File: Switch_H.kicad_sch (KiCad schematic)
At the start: 10 parts, among them Q501 NMOS, Q502 NMOS, U501 LM74700, U502 LM74700

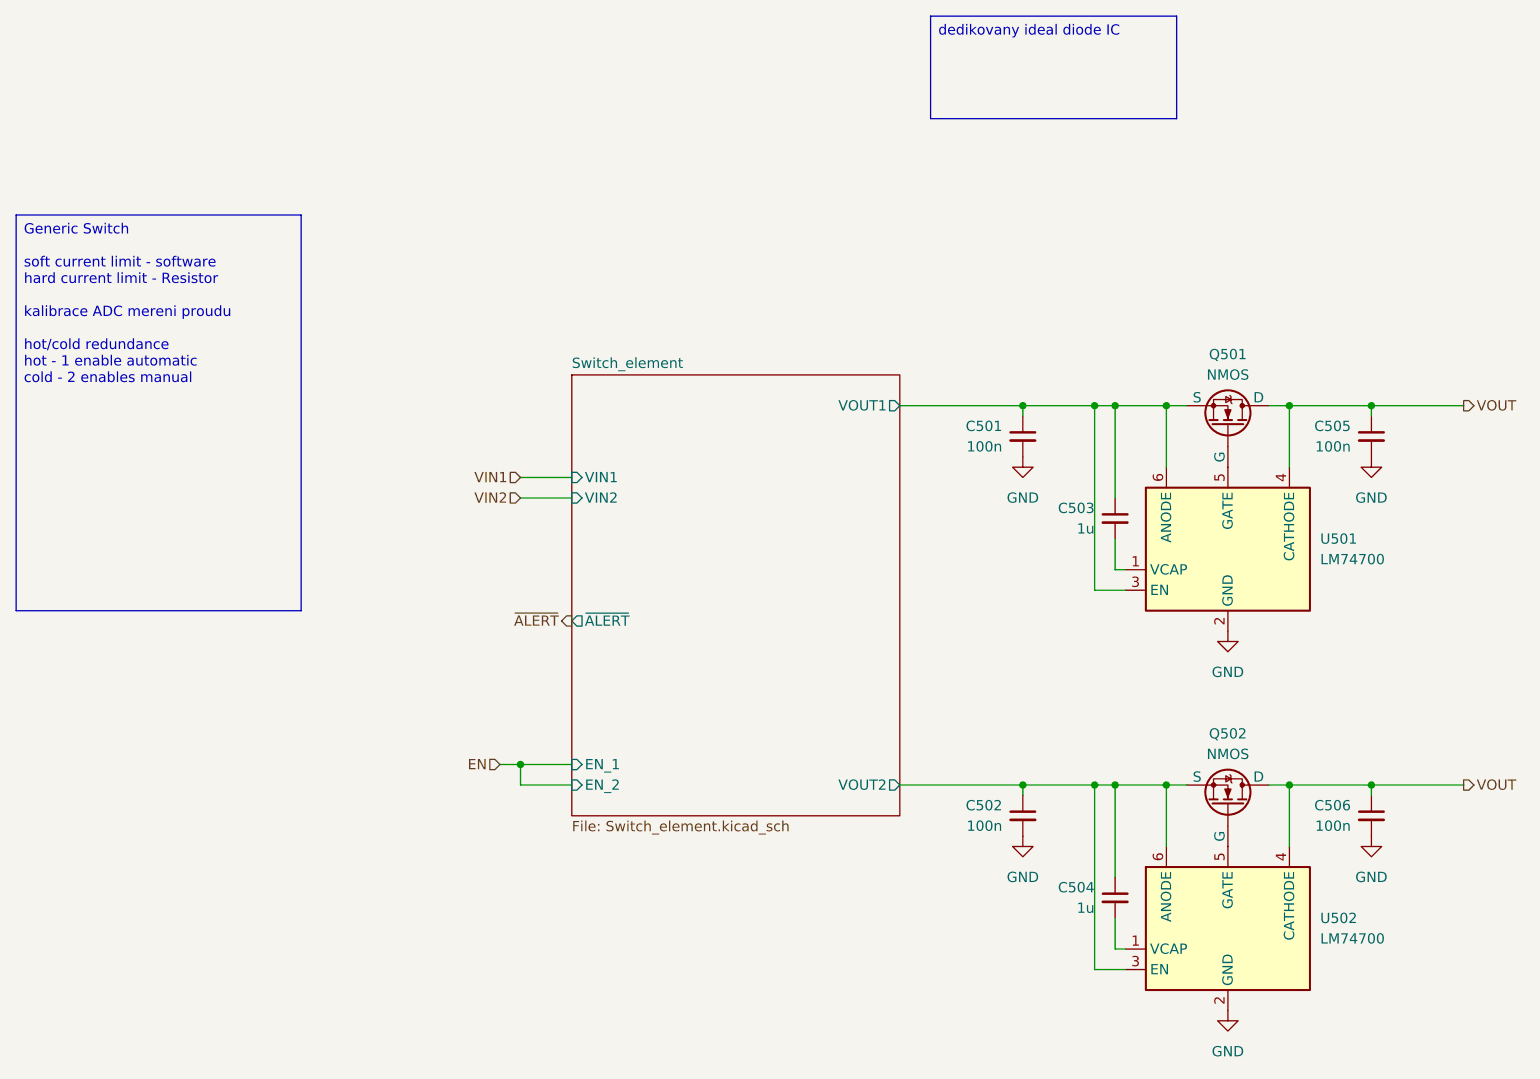
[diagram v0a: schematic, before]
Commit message: restructurization of the entire project improved
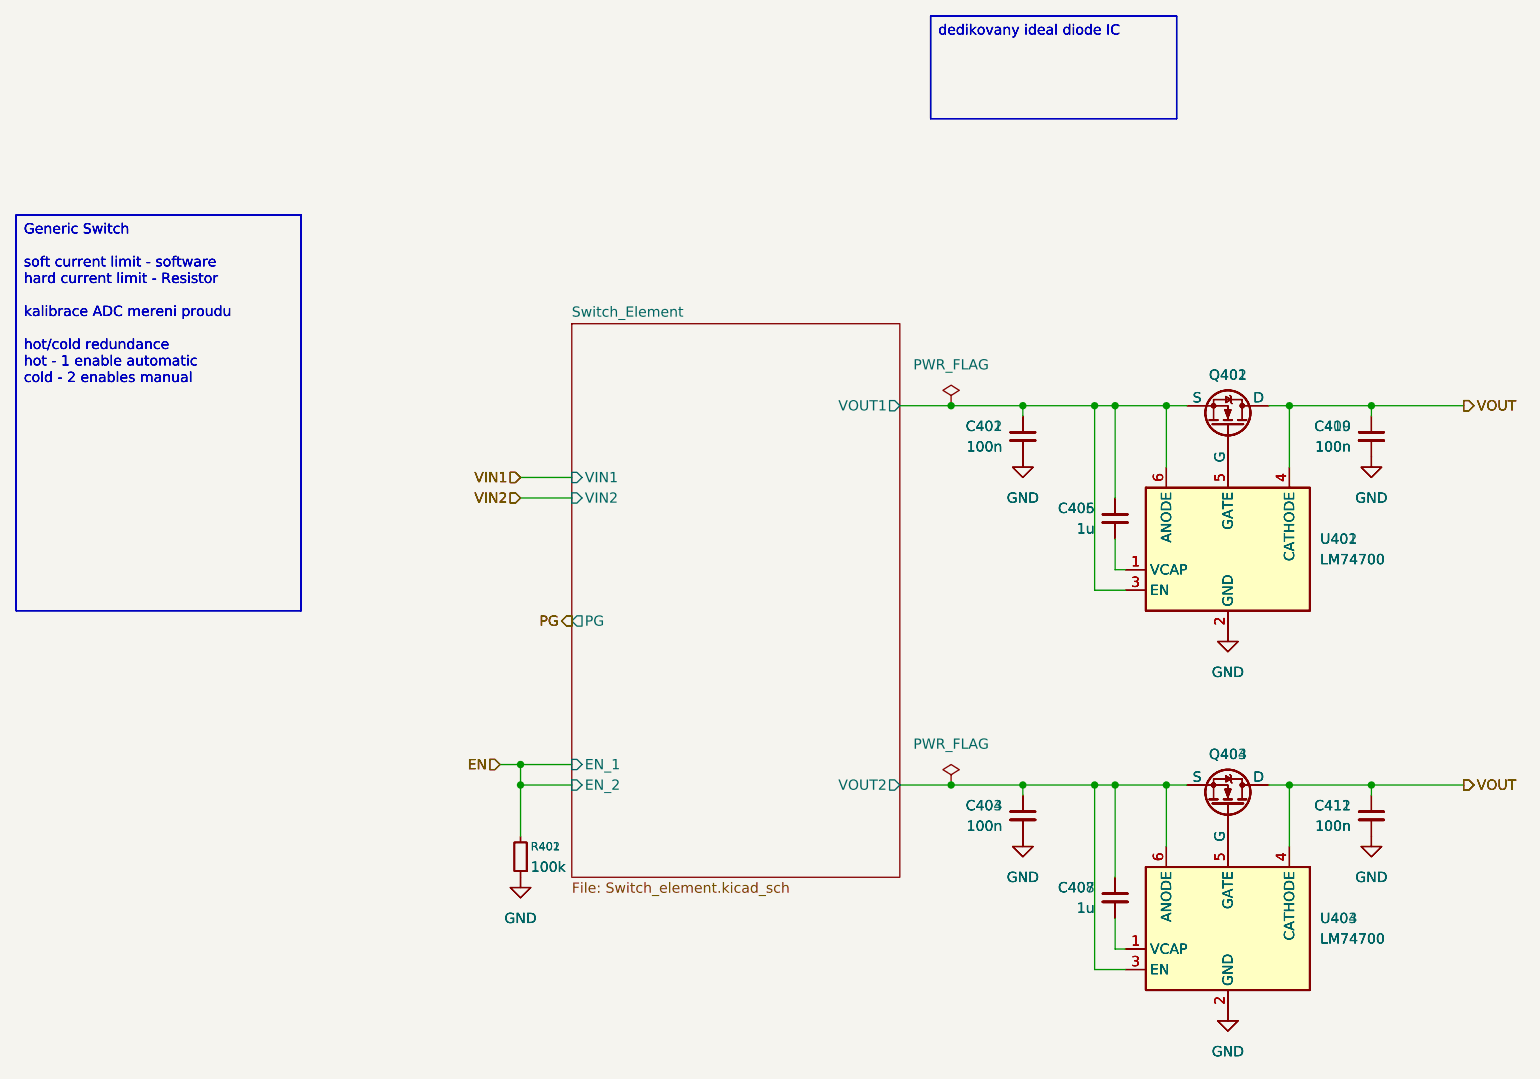
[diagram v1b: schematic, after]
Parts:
- added C402, C404, C410, C412: 100n, Capacitor_SMD:C_0603_1608Metric_Pad1.08x0.95mm_HandSolder, symbol Device:C_Small
- added C406, C408: 1u, Capacitor_SMD:C_0603_1608Metric_Pad1.08x0.95mm_HandSolder, symbol Device:C_Small
- added Q402, Q403: NVTFWS4D9N04XMTAG, Outlines:NVTFS5116PLTWG, symbol Simulation_SPICE:NMOS
- added R401, R402: 100k, Resistor_SMD:R_0603_1608Metric_Pad0.98x0.95mm_HandSolder, symbol Device:R_Small
- added U401, U403: LM74700, Package_TO_SOT_SMD:SOT-23-6, symbol Power_Management:LM74700
- Q401: renamed from Q501; value NMOS -> NVTFWS4D9N04XMTAG
- Q404: renamed from Q502; value NMOS -> NVTFWS4D9N04XMTAG
- renumbered C501 to C401, C502 to C403, C503 to C405, C504 to C407, C505 to C409, C506 to C411, U501 to U402, U502 to U404
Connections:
- net EN: now also R401.2, R402.2
- net GND: now also C402.2, C404.2, C410.2, C412.2, R401.1, R402.1, U401.2 (GND), U403.2 (GND)
- net VOUT: now also C410.1, C412.1, Q402.1 (D), Q403.1 (D), U401.4 (CATHODE), U403.4 (CATHODE)
- net at Q401.2 (G), U402.5 (GATE): now also Q402.2 (G), U401.5 (GATE)
- net at C407.2, U404.1 (VCAP): now also C408.2, U403.1 (VCAP)
- net at C405.2, U402.1 (VCAP): now also C406.2, U401.1 (VCAP)
- net at Q404.2 (G), U404.5 (GATE): now also Q403.2 (G), U403.5 (GATE)
- net Switch_element/VOUT1 renamed Switch_Element/VOUT1
- net Switch_Element/VOUT1: now also C402.1, C406.1, Q402.3 (S), U401.3 (EN), U401.6 (ANODE)
- net Switch_element/VOUT2 renamed Switch_Element/VOUT2
- net Switch_Element/VOUT2: now also C404.1, C408.1, Q403.3 (S), U403.3 (EN), U403.6 (ANODE)
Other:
- removed sheet Switch_element
- added sheet Switch_Element (Switch_element.kicad_sch)

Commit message: added universal switch, added simples current source, reworked test schematic and pcb
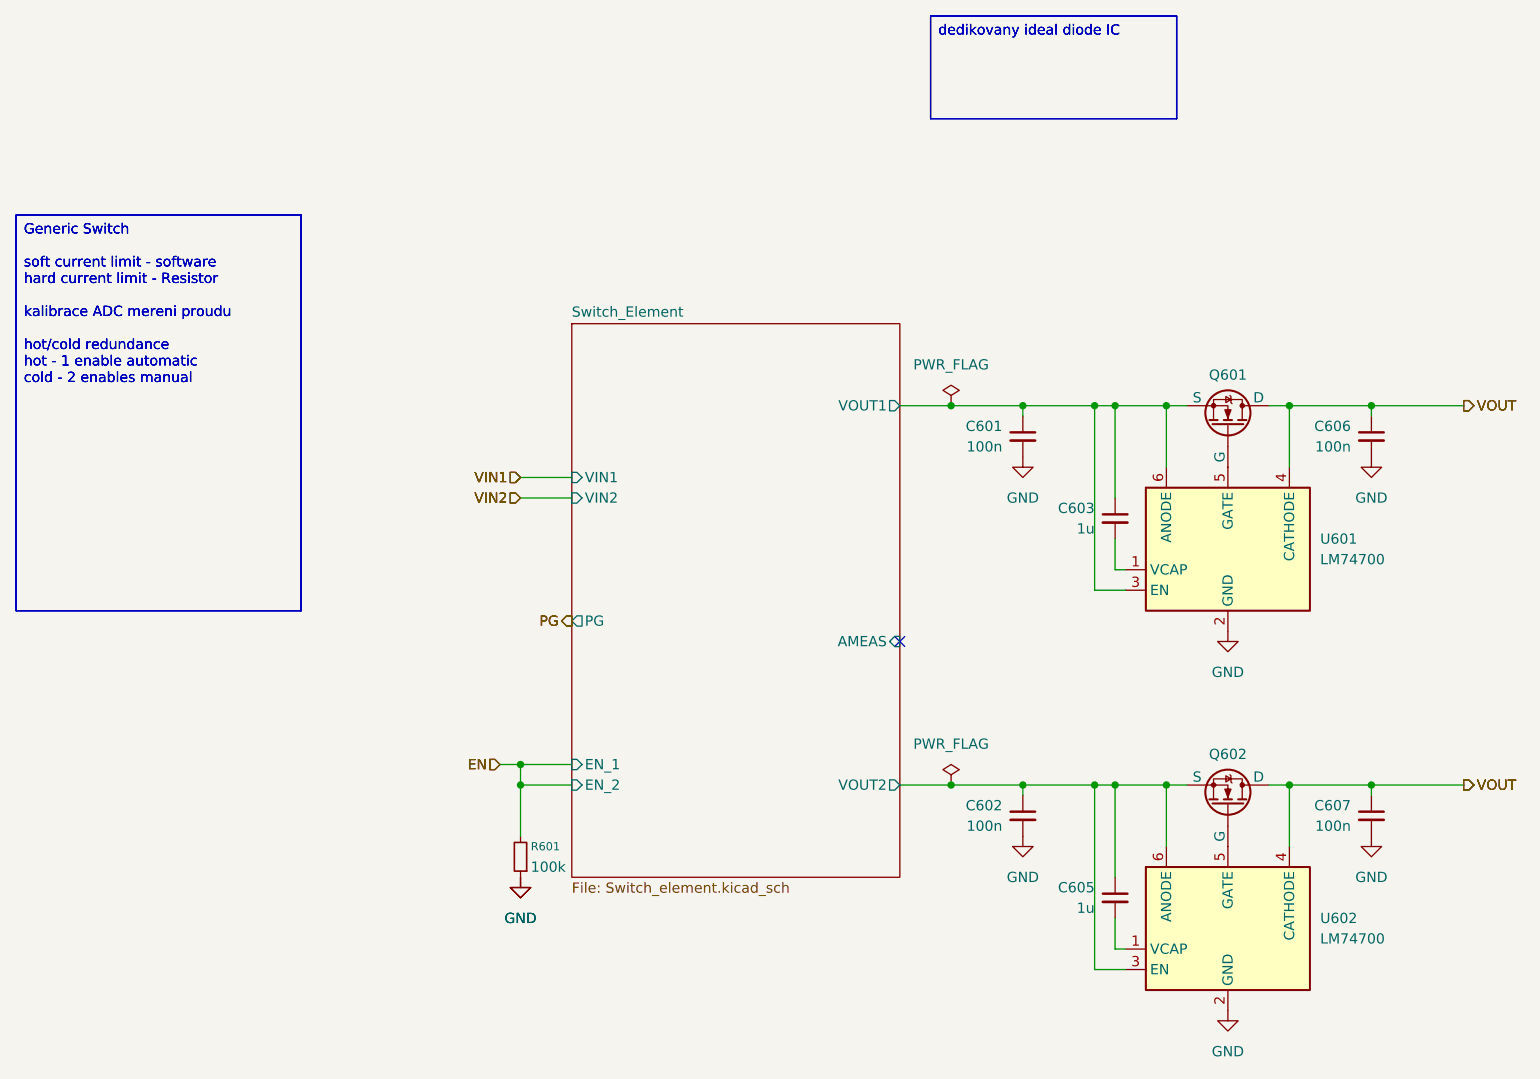
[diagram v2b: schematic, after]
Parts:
- removed C401, C404, C409, C411: 100n, Capacitor_SMD:C_0603_1608Metric_Pad1.08x0.95mm_HandSolder, symbol Device:C_Small
- removed C406, C407: 1u, Capacitor_SMD:C_0603_1608Metric_Pad1.08x0.95mm_HandSolder, symbol Device:C_Small
- removed Q402, Q403: NVTFWS4D9N04XMTAG, Outlines:NVTFS5116PLTWG, symbol Simulation_SPICE:NMOS
- removed R402: 100k, Resistor_SMD:R_0603_1608Metric_Pad0.98x0.95mm_HandSolder, symbol Device:R_Small
- removed U401, U404: LM74700, Package_TO_SOT_SMD:SOT-23-6, symbol Power_Management:LM74700
- renumbered C402 to C601, C403 to C602, C405 to C603, C408 to C605, C410 to C606, C412 to C607, Q401 to Q601, Q404 to Q602, R401 to R601, U402 to U601, U403 to U602
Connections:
- no-connect marks 0 -> 1
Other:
- sheet Switch_Element ports: added AMEAS; removed none

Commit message: progress on CORE pcb
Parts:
- renumbered C601 to C201, C606 to C202, C603 to C203, C602 to C204, C607 to C205, C605 to C206, Q601 to Q201, Q602 to Q202, R601 to R201, U601 to U201, U602 to U202
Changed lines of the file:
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@@
 		(dnp no)
 		(fields_autoplaced yes)
-		(property "Reference" "#PWR0607"
+		(property "Reference" "#PWR0136"
 			(at 191.77 76.2 0)
 			(effects
@@
 			(project "EPS_CORE"
 				(path "/43e5e7c8-e7e0-4528-9a3e-b1557849918d/698c15de-e9f5-4d16-9003-7ad12b03691d"
-					(reference "#PWR?")
+					(reference "#PWR0136")
 					(unit 1)
 				)
@@
 		(dnp no)
 		(fields_autoplaced yes)
-		(property "Reference" "#FLG0602"
+		(property "Reference" "#FLG0102"
 			(at 139.7 108.585 0)
 			(effects
@@
 			(project "EPS_CORE"
 				(path "/43e5e7c8-e7e0-4528-9a3e-b1557849918d/698c15de-e9f5-4d16-9003-7ad12b03691d"
-					(reference "#FLG?")
+					(reference "#FLG0102")
 					(unit 1)
 				)
@@
 		(dnp no)
 		(fields_autoplaced yes)
-		(property "Reference" "#FLG0601"
+		(property "Reference" "#FLG0101"
 			(at 139.7 61.595 0)
 			(effects
@@
 			(project "EPS_CORE"
 				(path "/43e5e7c8-e7e0-4528-9a3e-b1557849918d/698c15de-e9f5-4d16-9003-7ad12b03691d"
-					(reference "#FLG?")
+					(reference "#FLG0101")
 					(unit 1)
 				)
@@
 		(on_board yes)
 		(dnp no)
-		(property "Reference" "R601"
+		(property "Reference" "R201"
 			(at 87.63 118.11 0)
 			(effects
@@
 			(project "EPS_CORE"
 				(path "/43e5e7c8-e7e0-4528-9a3e-b1557849918d/698c15de-e9f5-4d16-9003-7ad12b03691d"
-					(reference "R?")
+					(reference "R201")
 					(unit 1)
 				)
@@
 		(on_board yes)
 		(dnp no)
-		(property "Reference" "Q601"
+		(property "Reference" "Q201"
 			(at 173.99 59.69 90)
 			(effects
@@
 			(project "EPS_CORE"
 				(path "/43e5e7c8-e7e0-4528-9a3e-b1557849918d/698c15de-e9f5-4d16-9003-7ad12b03691d"
-					(reference "Q?")
+					(reference "Q201")
 					(unit 1)
 				)
@@
 		(dnp no)
 		(fields_autoplaced yes)
-		(property "Reference" "#PWR0601"
+		(property "Reference" "#PWR0131"
 			(at 86.36 128.27 0)
 			(effects
@@
 			(project "EPS_CORE"
 				(path "/43e5e7c8-e7e0-4528-9a3e-b1557849918d/698c15de-e9f5-4d16-9003-7ad12b03691d"
-					(reference "#PWR?")
+					(reference "#PWR0131")
 					(unit 1)
 				)
@@
 		(dnp no)
 		(fields_autoplaced yes)
-		(property "Reference" "#PWR0605"
+		(property "Reference" "#PWR0133"
 			(at 173.99 97.79 0)
 			(effects
@@
 			(project "EPS_CORE"
 				(path "/43e5e7c8-e7e0-4528-9a3e-b1557849918d/698c15de-e9f5-4d16-9003-7ad12b03691d"
-					(reference "#PWR?")
+					(reference "#PWR0133")
 					(unit 1)
 				)
@@
 		(dnp no)
 		(fields_autoplaced yes)
-		(property "Reference" "#PWR0606"
+		(property "Reference" "#PWR0135"
 			(at 173.99 144.78 0)
 			(effects
@@
 			(project "EPS_CORE"
 				(path "/43e5e7c8-e7e0-4528-9a3e-b1557849918d/698c15de-e9f5-4d16-9003-7ad12b03691d"
-					(reference "#PWR?")
+					(reference "#PWR0135")
 					(unit 1)
 				)
@@
 		(dnp no)
 		(fields_autoplaced yes)
-		(property "Reference" "#PWR0603"
+		(property "Reference" "#PWR0137"
 			(at 148.59 76.2 0)
 			(effects
@@
 			(project "EPS_CORE"
 				(path "/43e5e7c8-e7e0-4528-9a3e-b1557849918d/698c15de-e9f5-4d16-9003-7ad12b03691d"
-					(reference "#PWR?")
+					(reference "#PWR0137")
 					(unit 1)
 				)
@@
 		(dnp no)
 		(fields_autoplaced yes)
-		(property "Reference" "#PWR0608"
+		(property "Reference" "#PWR0134"
 			(at 191.77 123.19 0)
 			(effects
@@
 			(project "EPS_CORE"
 				(path "/43e5e7c8-e7e0-4528-9a3e-b1557849918d/698c15de-e9f5-4d16-9003-7ad12b03691d"
-					(reference "#PWR?")
+					(reference "#PWR0134")
 					(unit 1)
 				)
@@
 		(dnp no)
 		(fields_autoplaced yes)
-		(property "Reference" "U602"
+		(property "Reference" "U202"
 			(at 185.42 126.9999 0)
 			(effects
@@
 			(project "EPS_CORE"
 				(path "/43e5e7c8-e7e0-4528-9a3e-b1557849918d/698c15de-e9f5-4d16-9003-7ad12b03691d"
-					(reference "U?")
+					(reference "U202")
 					(unit 1)
 				)
@@
 		(on_board yes)
 		(dnp no)
-		(property "Reference" "C602"
+		(property "Reference" "C204"
 			(at 146.05 113.0362 0)
 			(effects
@@
 			(project "EPS_CORE"
 				(path "/43e5e7c8-e7e0-4528-9a3e-b1557849918d/698c15de-e9f5-4d16-9003-7ad12b03691d"
-					(reference "C?")
+					(reference "C204")
 					(unit 1)
 				)
@@
 		(on_board yes)
 		(dnp no)
-		(property "Reference" "C603"
+		(property "Reference" "C203"
 			(at 157.48 76.2062 0)
 			(effects
@@
 			(project "EPS_CORE"
 				(path "/43e5e7c8-e7e0-4528-9a3e-b1557849918d/698c15de-e9f5-4d16-9003-7ad12b03691d"
-					(reference "C?")
+					(reference "C203")
 					(unit 1)
 				)
@@
 		(on_board yes)
 		(dnp no)
-		(property "Reference" "C601"
+		(property "Reference" "C201"
 			(at 146.05 66.0462 0)
 			(effects
@@
 			(project "EPS_CORE"
 				(path "/43e5e7c8-e7e0-4528-9a3e-b1557849918d/698c15de-e9f5-4d16-9003-7ad12b03691d"
-					(reference "C?")
+					(reference "C201")
 					(unit 1)
 				)
@@
 		(on_board yes)
 		(dnp no)
-		(property "Reference" "C606"
+		(property "Reference" "C202"
 			(at 189.23 66.0462 0)
 			(effects
@@
 			(project "EPS_CORE"
 				(path "/43e5e7c8-e7e0-4528-9a3e-b1557849918d/698c15de-e9f5-4d16-9003-7ad12b03691d"
-					(reference "C?")
+					(reference "C202")
 					(unit 1)
 				)
@@
 		(dnp no)
 		(fields_autoplaced yes)
-		(property "Reference" "#PWR0604"
+		(property "Reference" "#PWR0138"
 			(at 148.59 123.19 0)
 			(effects
@@
 			(project "EPS_CORE"
 				(path "/43e5e7c8-e7e0-4528-9a3e-b1557849918d/698c15de-e9f5-4d16-9003-7ad12b03691d"
-					(reference "#PWR?")
+					(reference "#PWR0138")
 					(unit 1)
 				)
@@
 		(on_board yes)
 		(dnp no)
-		(property "Reference" "C607"
+		(property "Reference" "C205"
 			(at 189.23 113.0362 0)
 			(effects
@@
 			(project "EPS_CORE"
 				(path "/43e5e7c8-e7e0-4528-9a3e-b1557849918d/698c15de-e9f5-4d16-9003-7ad12b03691d"
-					(reference "C?")
+					(reference "C205")
 					(unit 1)
 				)
@@
 		(on_board yes)
 		(dnp no)
-		(property "Reference" "Q602"
+		(property "Reference" "Q202"
 			(at 173.99 106.68 90)
 			(effects
@@
 			(project "EPS_CORE"
 				(path "/43e5e7c8-e7e0-4528-9a3e-b1557849918d/698c15de-e9f5-4d16-9003-7ad12b03691d"
-					(reference "Q?")
+					(reference "Q202")
 					(unit 1)
 				)
@@
 		(dnp no)
 		(fields_autoplaced yes)
-		(property "Reference" "U601"
+		(property "Reference" "U201"
 			(at 185.42 80.0099 0)
 			(effects
@@
 			(project "EPS_CORE"
 				(path "/43e5e7c8-e7e0-4528-9a3e-b1557849918d/698c15de-e9f5-4d16-9003-7ad12b03691d"
-					(reference "U?")
+					(reference "U201")
 					(unit 1)
 				)
@@
 		(dnp no)
 		(fields_autoplaced yes)
-		(property "Reference" "#PWR0602"
+		(property "Reference" "#PWR0132"
 			(at 86.36 128.27 0)
 			(effects
@@
 			(project "EPS_CORE"
 				(path "/43e5e7c8-e7e0-4528-9a3e-b1557849918d/698c15de-e9f5-4d16-9003-7ad12b03691d"
-					(reference "#PWR?")
+					(reference "#PWR0132")
 					(unit 1)
 				)
@@
 		(on_board yes)
 		(dnp no)
-		(property "Reference" "C605"
+		(property "Reference" "C206"
 			(at 157.48 123.1962 0)
 			(effects
@@
 			(project "EPS_CORE"
 				(path "/43e5e7c8-e7e0-4528-9a3e-b1557849918d/698c15de-e9f5-4d16-9003-7ad12b03691d"
-					(reference "C?")
-					(unit 1)
-				)
+					(reference "C206")
+					(unit 1)
+				)
